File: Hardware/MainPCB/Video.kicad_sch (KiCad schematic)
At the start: 35 parts, among them U1 THS7374, U2 LMH1251MT_NOPB, U3 MAX4887, U4 MAX4887

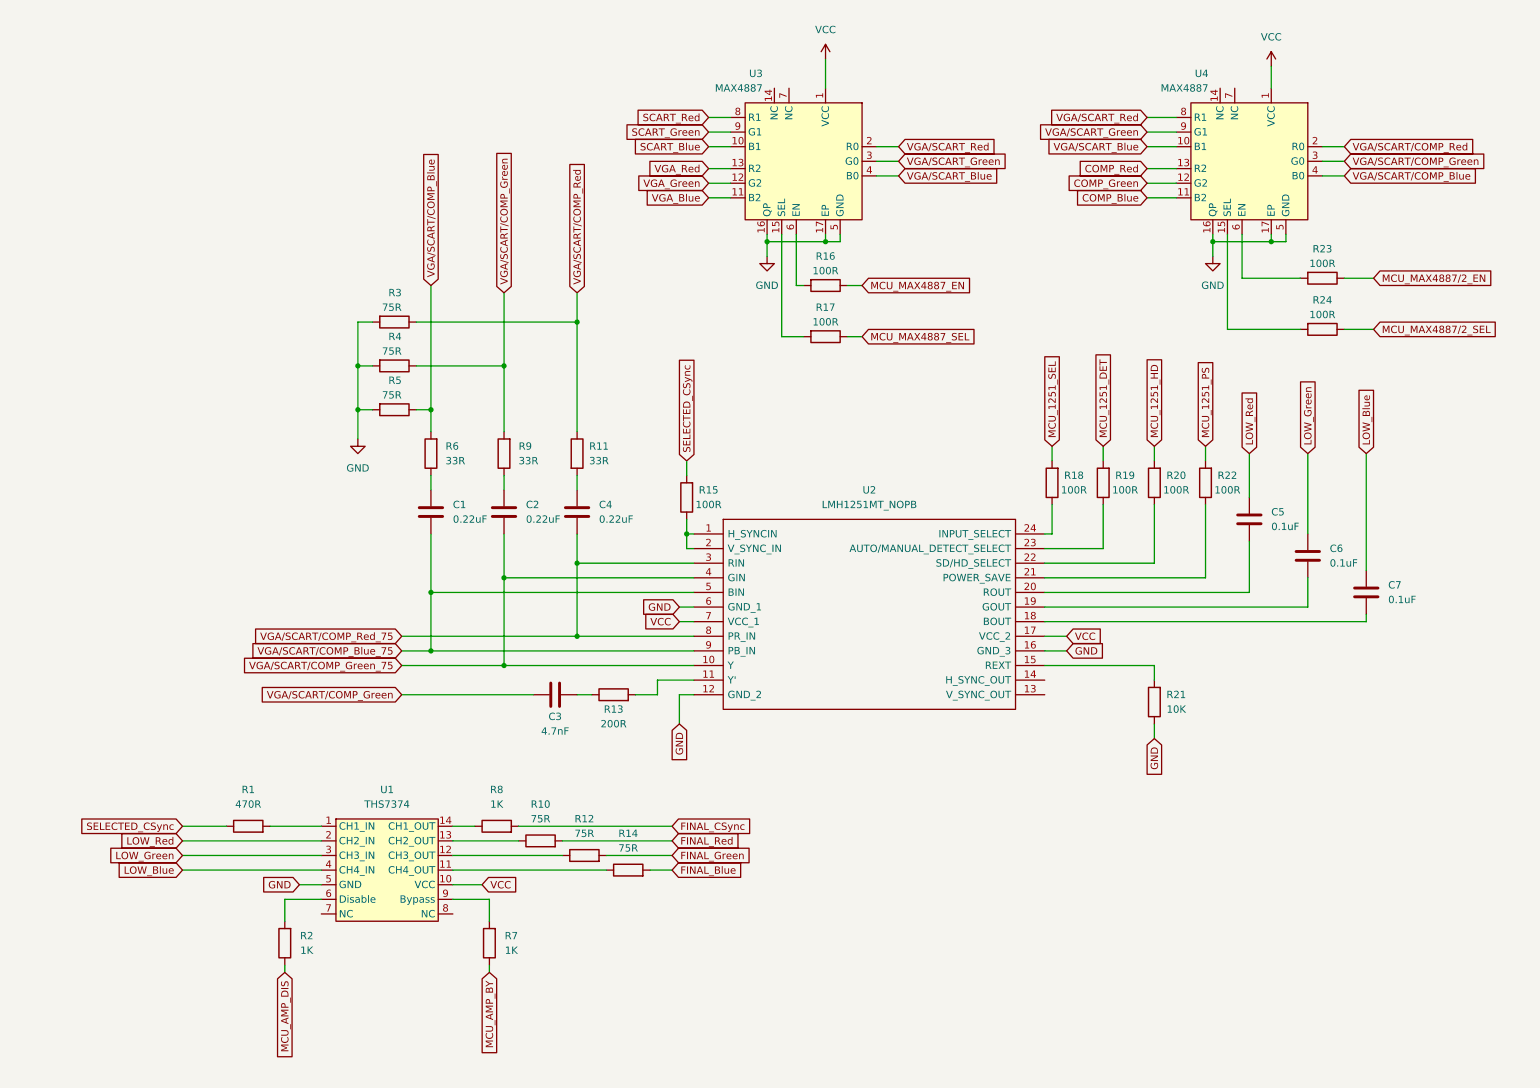
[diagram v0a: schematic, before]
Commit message: Fixed color bending issue; Added diagnostics
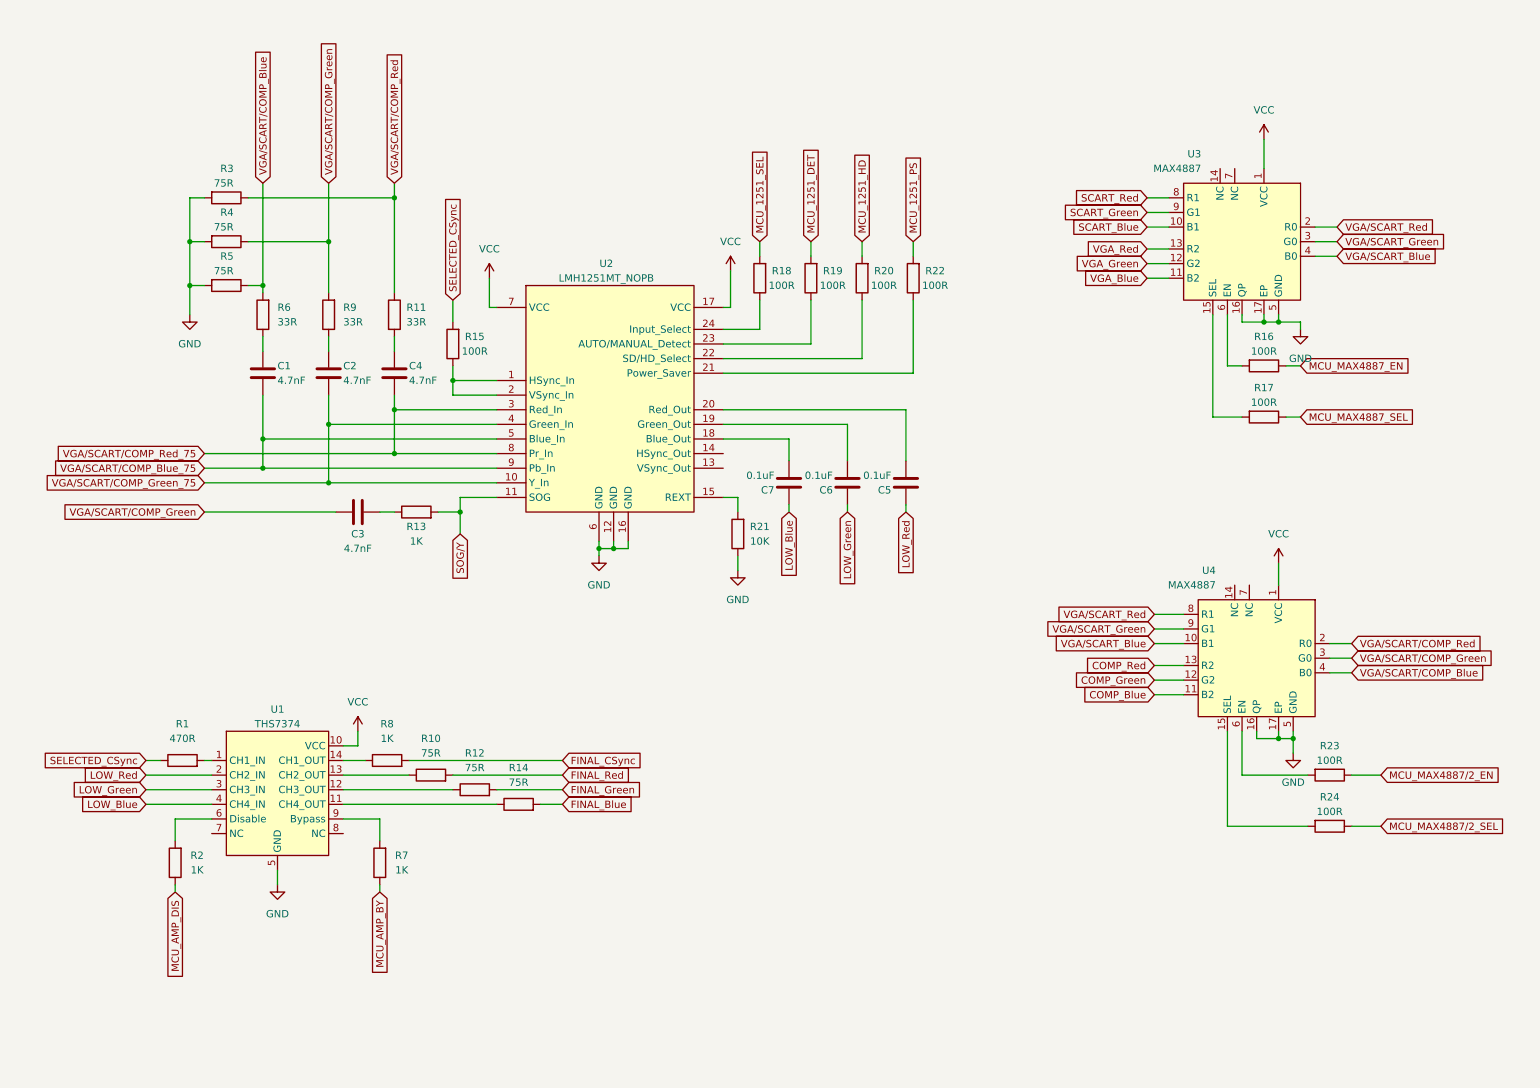
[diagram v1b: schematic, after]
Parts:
- C1, C2, C4: value 0.22uF -> 4.7nF
- R1, R10, R11, R12, R14, R15, R16, R17, R18, R19, R2, R20, R21, R22, R23, R24, R3, R4, R5, R6, R7, R8, R9: footprint Resistor_SMD:R_0603_1608Metric -> RT5XP-EXP:R_0603; symbol Device:R -> RT5XP_EXP:R
- R13: value 200R -> 1K; footprint Resistor_SMD:R_0603_1608Metric -> RT5XP-EXP:R_0603; symbol Device:R -> RT5XP_EXP:R
- U1: footprint Package_SO:TSSOP-14_4.4x5mm_P0.65mm -> RT5XP-EXP:TSSOP-14_4.4x5mm_P0.65mm; symbol AE:THS7374 -> RT5XP_EXP:THS7374
- U2: footprint Package_SO:TSSOP-24_4.4x7.8mm_P0.65mm -> RT5XP-EXP:TSSOP-24_4.4x7.8mm_P0.65mm; symbol LMH1251:LMH1251MT_NOPB -> RT5XP_EXP:LMH1251; Height 1.2 -> (none); Manufacturer_Name Texas Instruments -> (none); Manufacturer_Part_Number LMH1251MT/NOPB -> (none); Mouser Part Number 926-LMH1251MT/NOPB -> (none); Mouser Price/Stock https://www.mouser.co.uk/ProductDetail/Texas-Instruments/LM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 -> (none)
- U3, U4: footprint Package_DFN_QFN:TQFN-16-1EP_3x3mm_P0.5mm_EP1.23x1.23mm -> RT5XP-EXP:TQFN-16-1EP_3x3mm_P0.5mm_EP1.23x1.23mm; symbol AE:MAX4887 -> RT5XP_EXP:MAX4887
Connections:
- net SOG/Y: now reaches R13.2, U2.11 (SOG)
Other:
- moved on the sheet: C1, C2, C3, C4, C5, C6, C7, R1, R10, R11, R12, R13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
